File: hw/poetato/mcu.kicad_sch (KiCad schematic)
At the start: 89 parts, among them J3 FTSH-105-01-L-DV-007-K, J4 61300611121, J8 614105150721, Q10 NTK3134N, Q9 NTK3134N, U1 MCXN247VKLT, U10 SE051, U11 S25FL064LABMFI013, U2 LP3470A293DBVR, U20 USBLC6-4, U8 USBLC6-4, U9 USBLC6-4, Y1 32.768kHz, Y3 24MHz

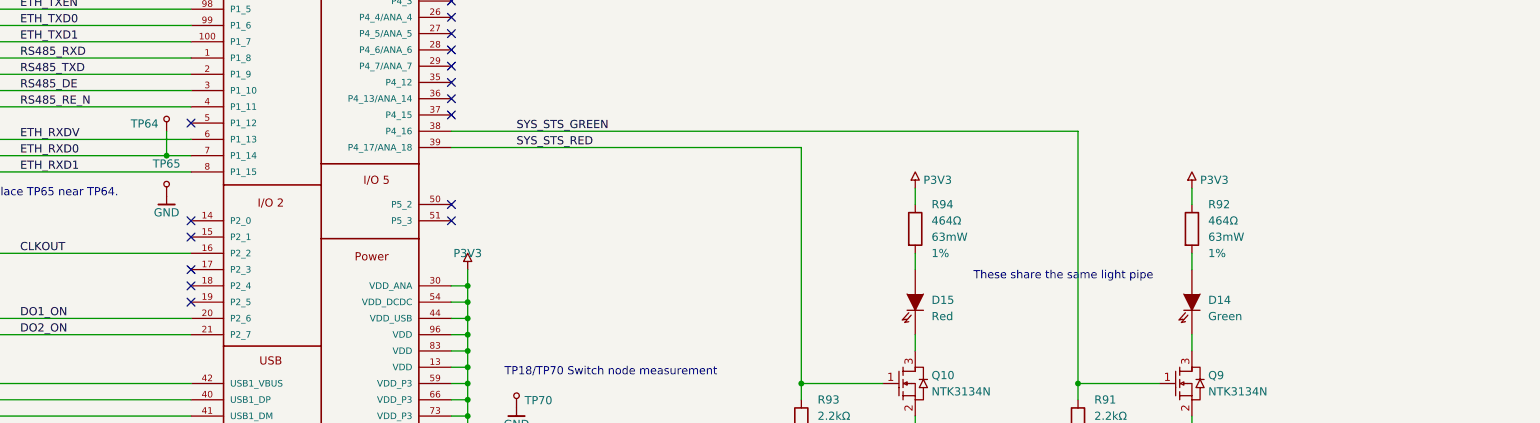
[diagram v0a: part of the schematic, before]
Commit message: hw: fix local text collisions and add strap and BOM notes
- MCU: light-pipe note beside D14, TP64/TP65 references off the signal rows
- Ethernet: KSZ8081 strap summary (PHY address 1, RMII, auto-neg 100M),
  TP6 reference clear of POE_VDD
- IO: rating notes merged into the notes box
- DO: PhotoMOS note under K1
- Top level: frame and title around the BOM-only entries

Text and graphics only; ERC clean, netlist unchanged.
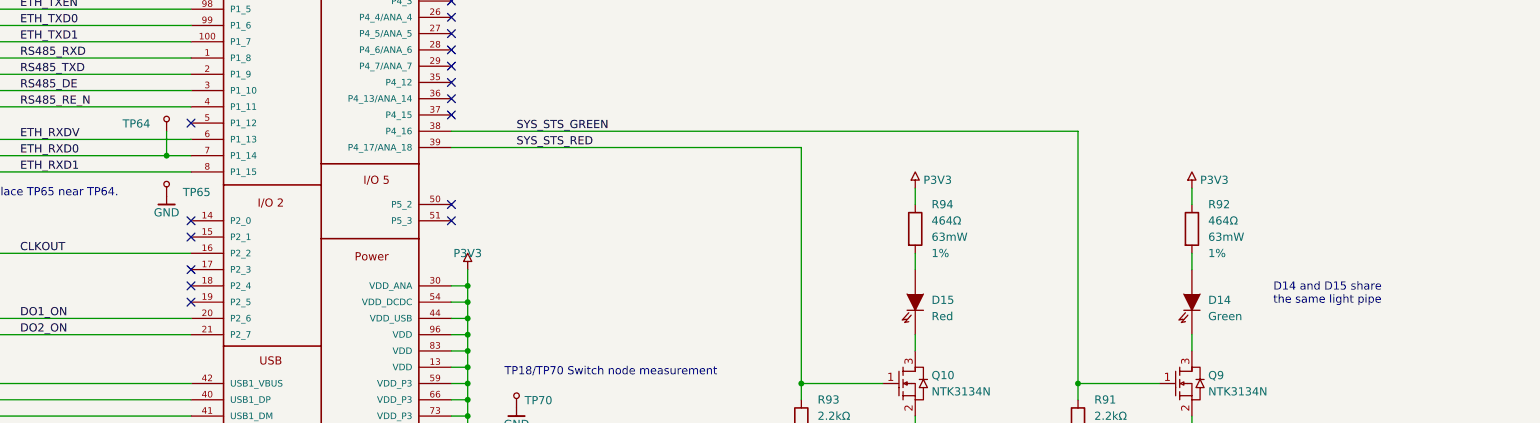
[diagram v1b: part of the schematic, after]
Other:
- note added: "D14 and D15 share the same light pipe"
- note removed: "These share the same light pipe"
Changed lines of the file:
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@@
 		)
 	)
-	(text "These share the same light pipe"
+	(text "D14 and D15 share\nthe same light pipe"
 		(exclude_from_sim no)
-		(at 306.324 163.576 0)
+		(at 339.09 166.37 0)
 		(effects
 			(font
 				(size 1.27 1.27)
 			)
+			(justify left)
 		)
 	)
@@
 		(fields_autoplaced yes)
 		(property "Reference" "TP65"
-			(at 166.37 146.05 0)
+			(at 168.91 150.495 0)
 			(show_name no)
 			(do_not_autoplace no)
@@
 					(size 1.27 1.27)
 				)
+				(justify left)
 			)
 		)
@@
 		(fields_autoplaced yes)
 		(property "Reference" "TP64"
-			(at 165.1 139.8015 0)
+			(at 163.83 139.8 0)
 			(show_name no)
 			(do_not_autoplace no)

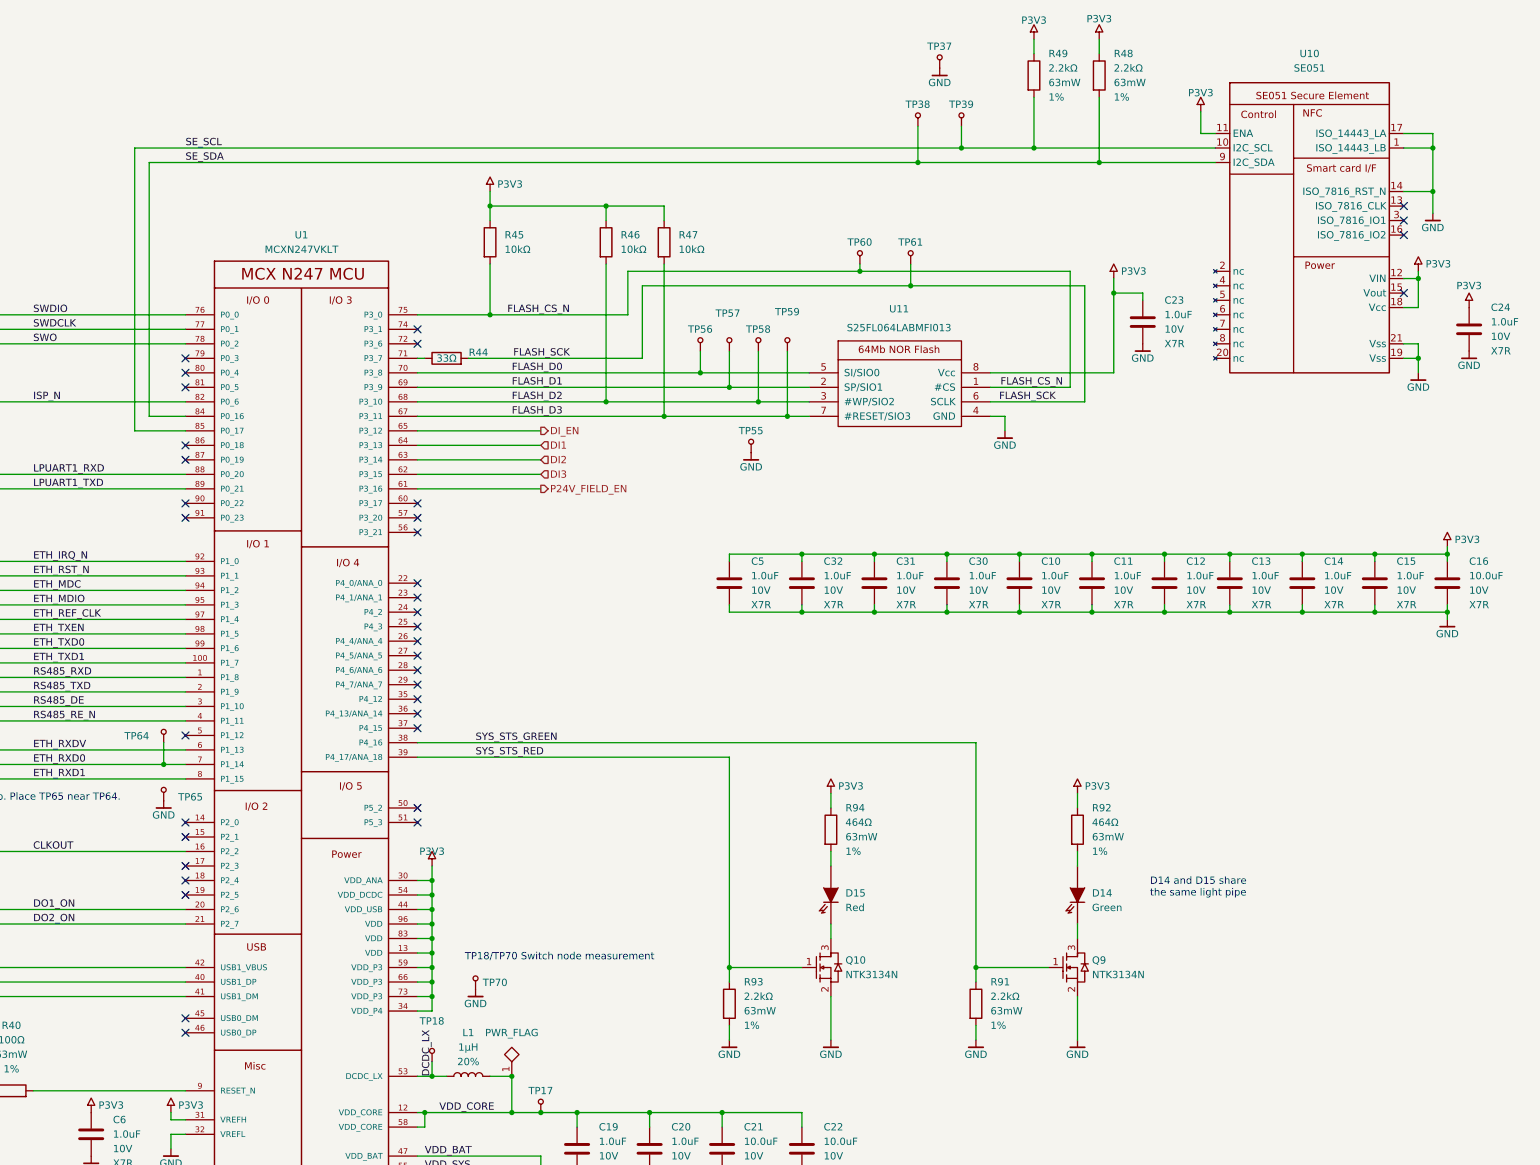
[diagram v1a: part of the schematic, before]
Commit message: hw: move flash, SE051 and status LEDs to an MCU peripherals sub-sheet
mcu_periph.kicad_sch (/MCU/Peripherals/, A4, page 3) holds U11 with its
pull-ups and test points, U10 with the I2C pull-ups, and the two status
LED drivers. U1 connects to it through short labelled stubs, which
removes the SE_SCL/SE_SDA route over the top of the MCU sheet and the
long SYS_STS wires. R44 stays next to U1.

Symbols keep their UUIDs and references; netlist unchanged including
net names. Later pages move down by one.
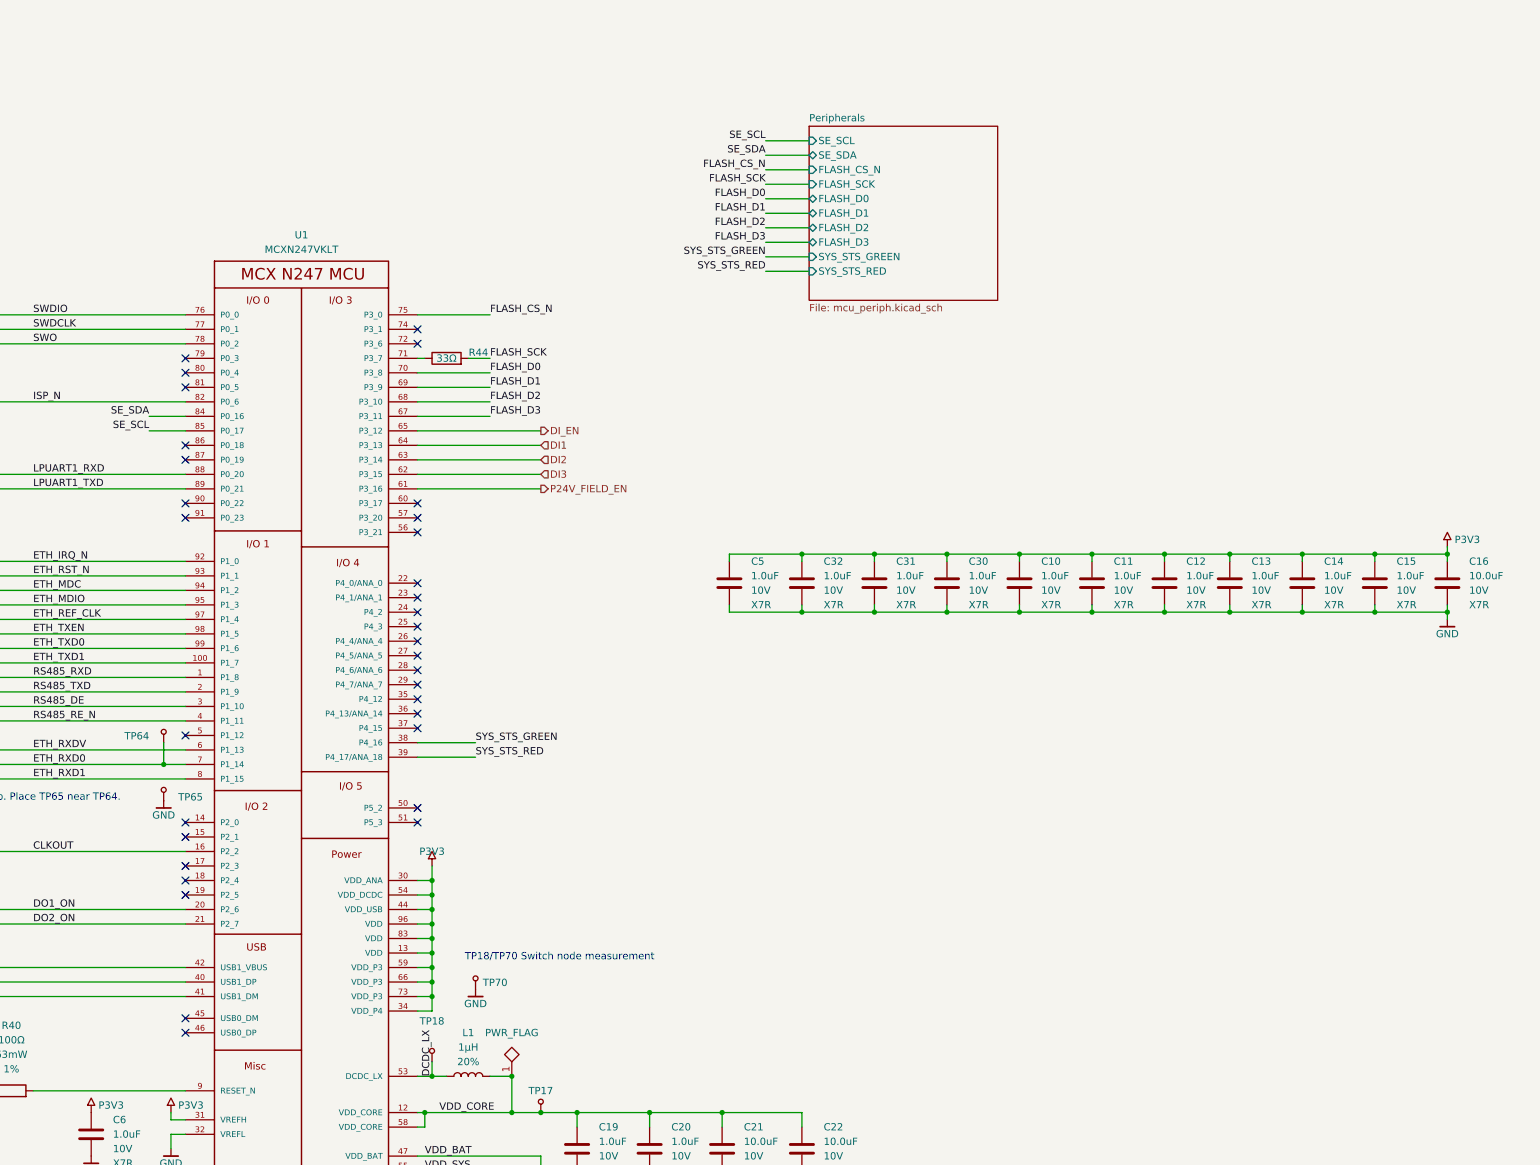
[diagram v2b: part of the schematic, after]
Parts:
- removed C23, C24: ${Capacitance}, Capacitor_SMD:C_0402_1005Metric, symbol cap_mlcc_murata_GRM:GRM/C0402_1u_10V_X7R_10%
- removed D14: LED0402_150040VS73240, LED_SMD:LED_0402_1005Metric, symbol LEDs:LED0402_150040VS73240
- removed D15: LED0402_150040SS73240, LED_SMD:LED_0402_1005Metric, symbol LEDs:LED0402_150040SS73240
- removed Q10, Q9: NTK3134N, Package_TO_SOT_SMD:SOT-723, symbol transistors:NTK3134N
- removed R45, R46, R47: 10kΩ, Resistor_SMD:R_0402_1005Metric, symbol res_chip_vishay_crcw:CRCW/R0402_10k0_1_63mW
- removed R48, R49, R91, R93: 2.2kΩ, Resistor_SMD:R_0402_1005Metric, symbol res_chip_vishay_crcw:CRCW/R0402_2k2_1_63mW
- removed R92, R94: 464Ω, Resistor_SMD:R_0402_1005Metric, symbol res_chip_vishay_crcw:CRCW/R0402_464R0_1_63mW
- removed TP37, TP38, TP39, TP55, TP56, TP57, TP58, TP59, TP60, TP61: TP, TestPoint:TestPoint_Pad_D1.0mm, symbol power:TP
- removed U10: SE051, Package_DFN_QFN:UQFN-20-1EP_3x3mm_P0.4mm_EP1.85x1.85mm, symbol comm:SE051C2HQ1
- removed U11: S25FL064LABMFI013, Package_SO:SOIC-8_5.3x5.3mm_P1.27mm, symbol memory:S25FL064LABMFI013
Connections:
- no-connect marks 45 -> 41
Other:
- added sheet Peripherals (mcu_periph.kicad_sch)
- note removed: "D14 and D15 share the same light pipe"
- title: PoEtato - MCU, secure element and flash -> PoEtato - MCU core, debug and USB

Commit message: hw: schematic touch-ups, J3 updated from library
Layout touch-ups in KiCad. J3 (FTSH-105) pulled from kicadlib 81de170:
pin numbers without leading zeros (01-10 -> 1-10). Otherwise connectivity
and values unchanged; ERC clean. Project file picks up the Peripherals
sheet name.
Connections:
- net GND: now also J3.3, J3.5, J3.9; no longer J3.03, J3.05, J3.09
- net SWDCLK: now also J3.4; no longer J3.04
- net SWDIO: now also J3.2; no longer J3.02
- net SWO: now also J3.6; no longer J3.06
- net at R29.2: now also J3.1; no longer J3.01
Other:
- moved on the sheet: C10, C11, C12, C13, C14, C15, C16, C30, C31, C32, C5

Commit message: hw: 2.54 mm block titles, DI sheets on A3
- MCU: RTC block title at 2.54 mm (two lines); its contents move down
  7.62 mm to make room
- Peripherals: the three block titles at 2.54 mm, left-aligned in their frames
- DI: A3 like every other sheet, content placed as on the DO sheets; the
  COOL_POUR ERC exclusion in the project file follows the label

ERC clean, netlist unchanged.
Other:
- note added: "RTC & SRAM backup (≥ 8 h)"
- note removed: "RTC & SRAM Backup power (>= 8h)"
- moved on the sheet: C33, C9, D17, R50, TP16, TP36

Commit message: hw, doc: design rules and impedance net classes
Net classes 50Ohm_RMII, 50Ohm_QSPI, 90Ohm-diff_USB, 100Ohm-diff_MDI,
assigned in the schematic: hidden Netclass fields on the labels, two
rule areas for the PHY-side RMII stubs, ETH_REF_CLK_PHY label after
R26. USB_DP/USB_DM renamed USB_D_P/USB_D_N so KiCad pairs them.

Board rules per doc/pcb-stackup.md section 8: 0.12 mm min track,
0.18 default, 0.15 clearance, vias 0.3/0.6 (0.25/0.45 small), silk and
mask minimums, diff pair presets. poetato.kicad_dru holds the narrower
L3 widths. Unused inner-layer pads removed on all vias. Fab notes:
plain vias, no IPC-4761 Type VII required.
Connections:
- net USB_DM renamed USB_D_N
- net USB_DP renamed USB_D_P
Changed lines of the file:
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@@
 			(justify right bottom)
+		)
+		(property "Netclass" "50Ohm_QSPI"
+			(at 251.46 76.2 0)
+			(effects
+				(font
+					(size 1.27 1.27)
+					(italic yes)
+				)
+				(justify left)
+				(hide yes)
+			)
 		)
 	)
@@
 			(justify right bottom)
 		)
+		(property "Netclass" "50Ohm_QSPI"
+			(at 251.46 71.12 0)
+			(effects
+				(font
+					(size 1.27 1.27)
+					(italic yes)
+				)
+				(justify left)
+				(hide yes)
+			)
+		)
 	)
 	(label "DO2_ON"
@@
 			(justify right bottom)
 		)
+		(property "Netclass" "50Ohm_QSPI"
+			(at 251.46 81.28 0)
+			(effects
+				(font
+					(size 1.27 1.27)
+					(italic yes)
+				)
+				(justify left)
+				(hide yes)
+			)
+		)
 	)
 	(label "DCDC_LX"
@@
 			(justify right bottom)
 		)
+		(property "Netclass" "50Ohm_QSPI"
+			(at 251.46 73.66 0)
+			(effects
+				(font
+					(size 1.27 1.27)
+					(italic yes)
+				)
+				(justify left)
+				(hide yes)
+			)
+		)
 	)
 	(label "FLASH_CS_N"
@@
 			(justify right bottom)
 		)
+		(property "Netclass" "50Ohm_QSPI"
+			(at 252.73 63.5 0)
+			(effects
+				(font
+					(size 1.27 1.27)
+					(italic yes)
+				)
+				(justify left)
+				(hide yes)
+			)
+		)
 	)
 	(label "RS485_RXD"
@@
 			(justify right bottom)
 		)
+		(property "Netclass" "50Ohm_QSPI"
+			(at 251.46 78.74 0)
+			(effects
+				(font
+					(size 1.27 1.27)
+					(italic yes)
+				)
+				(justify left)
+				(hide yes)
+			)
+		)
 	)
 	(label "ETH_RXD1"
@@
 		)
 	)
-	(label "USB_DM"
+	(label "USB_D_N"
 		(at 46.99 185.42 0)
 		(effects
@@
 			(justify left bottom)
 		)
-	)
-	(label "USB_DP"
+		(property "Netclass" "90Ohm-diff_USB"
+			(at 46.99 182.88 0)
+			(effects
+				(font
+					(size 1.27 1.27)
+					(italic yes)
+				)
+				(justify left)
+				(hide yes)
+			)
+		)
+	)
+	(label "USB_D_P"
 		(at 46.99 182.88 0)
 		(effects
@@
 			(justify left bottom)
 		)
-	)
+		(property "Netclass" "90Ohm-diff_USB"
+			(at 46.99 180.34 0)
+			(effects
+				(font
+					(size 1.27 1.27)
+					(italic yes)
+				)
+				(justify left)
+				(hide yes)
+			)
+		)
+	)
